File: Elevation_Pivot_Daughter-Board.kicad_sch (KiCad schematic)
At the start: 0 parts

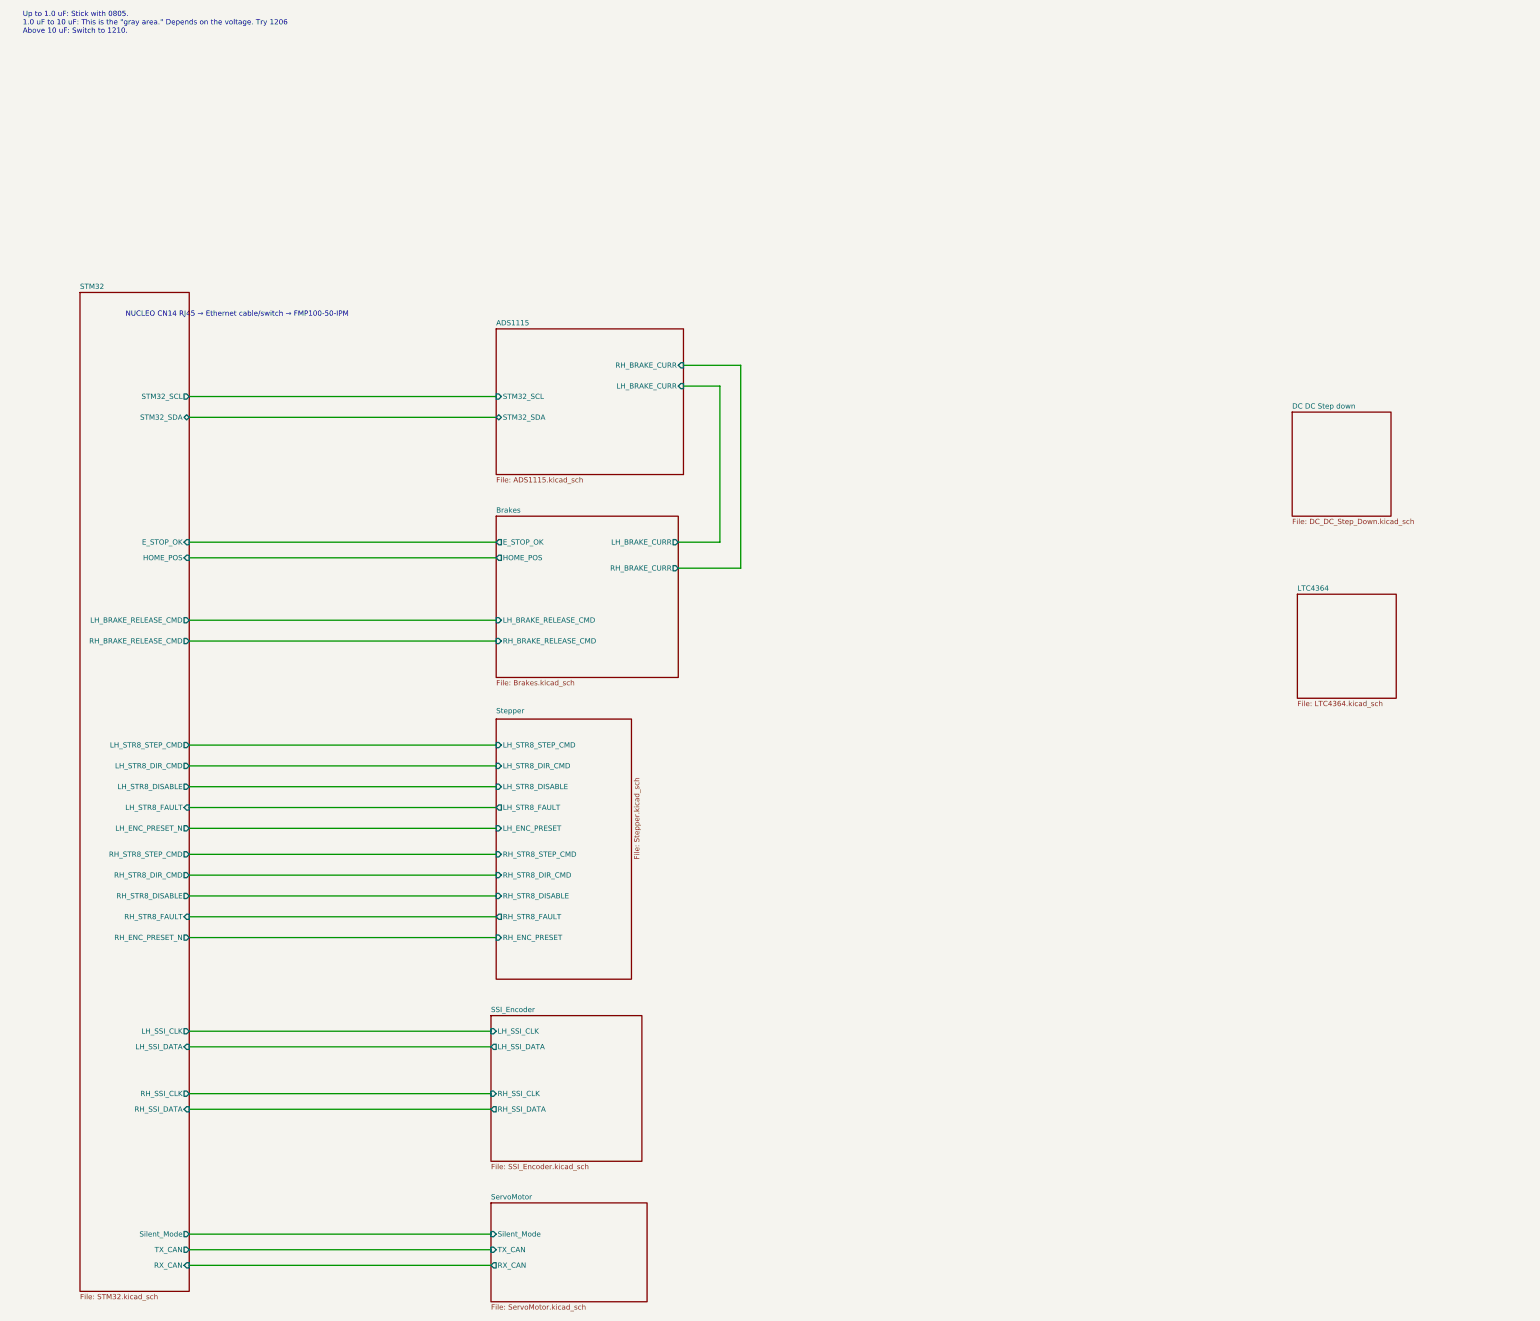
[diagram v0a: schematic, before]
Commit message: Redesign schematic for dual motor encoders
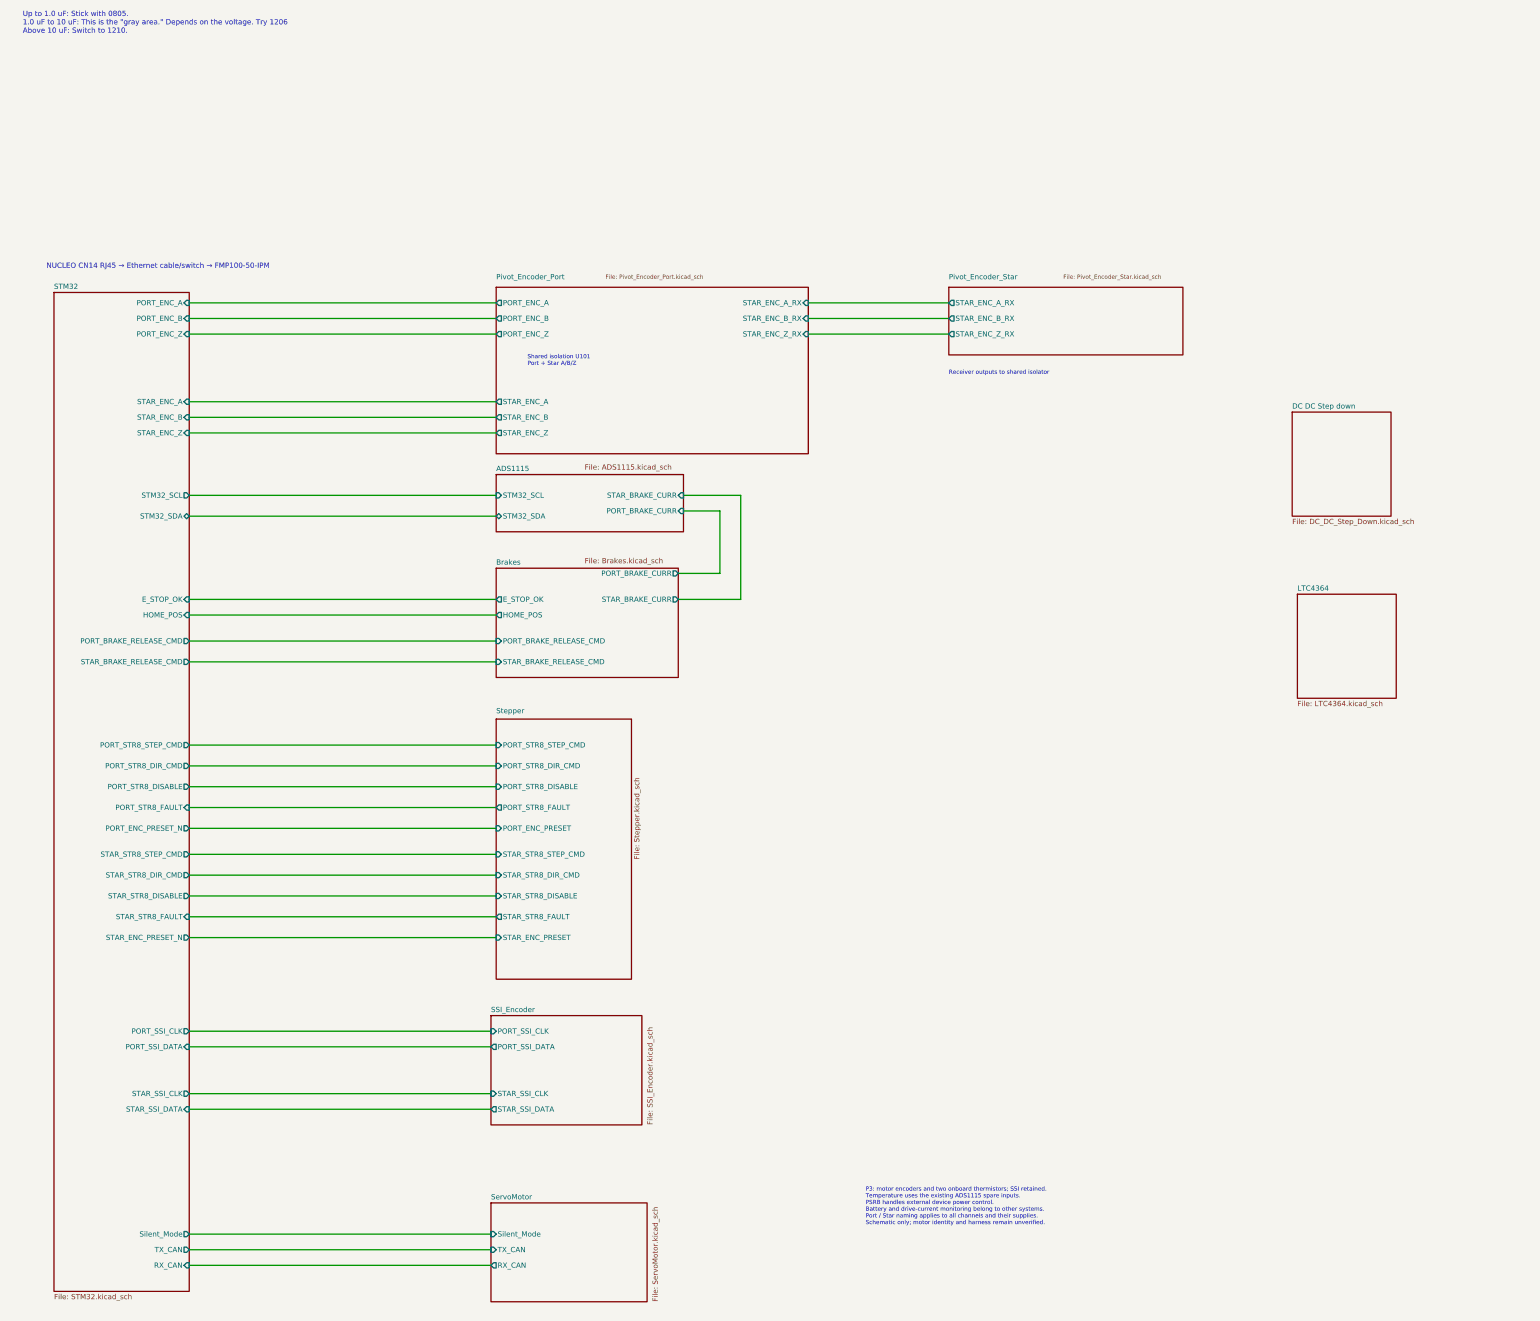
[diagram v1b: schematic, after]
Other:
- added sheet Pivot_Encoder_Port (Pivot_Encoder_Port.kicad_sch)
- added sheet Pivot_Encoder_Star (Pivot_Encoder_Star.kicad_sch)
- sheet ADS1115 ports: added PORT_BRAKE_CURR, STAR_BRAKE_CURR; removed LH_BRAKE_CURR, RH_BRAKE_CURR
- sheet Brakes ports: added PORT_BRAKE_CURR, PORT_BRAKE_RELEASE_CMD, STAR_BRAKE_CURR, STAR_BRAKE_RELEASE_CMD; removed LH_BRAKE_CURR, LH_BRAKE_RELEASE_CMD, RH_BRAKE_CURR, RH_BRAKE_RELEASE_CMD
- sheet SSI_Encoder ports: added PORT_SSI_CLK, PORT_SSI_DATA, STAR_SSI_CLK, STAR_SSI_DATA; removed LH_SSI_CLK, LH_SSI_DATA, RH_SSI_CLK, RH_SSI_DATA
- sheet STM32 ports: added PORT_BRAKE_RELEASE_CMD, PORT_ENC_A, PORT_ENC_B, PORT_ENC_PRESET_N, PORT_ENC_Z, PORT_SSI_CLK, PORT_SSI_DATA, PORT_STR8_DIR_CMD, PORT_STR8_DISABLE, PORT_STR8_FAULT, PORT_STR8_STEP_CMD, STAR_BRAKE_RELEASE_CMD, STAR_ENC_A, STAR_ENC_B, STAR_ENC_PRESET_N, STAR_ENC_Z, STAR_SSI_CLK, STAR_SSI_DATA, STAR_STR8_DIR_CMD, STAR_STR8_DISABLE, STAR_STR8_FAULT, STAR_STR8_STEP_CMD; removed LH_BRAKE_RELEASE_CMD, LH_ENC_PRESET_N, LH_SSI_CLK, LH_SSI_DATA, LH_STR8_DIR_CMD, LH_STR8_DISABLE, LH_STR8_FAULT, LH_STR8_STEP_CMD, RH_BRAKE_RELEASE_CMD, RH_ENC_PRESET_N, RH_SSI_CLK, RH_SSI_DATA, RH_STR8_DIR_CMD, RH_STR8_DISABLE, RH_STR8_FAULT, RH_STR8_STEP_CMD
- sheet Stepper ports: added PORT_ENC_PRESET, PORT_STR8_DIR_CMD, PORT_STR8_DISABLE, PORT_STR8_FAULT, PORT_STR8_STEP_CMD, STAR_ENC_PRESET, STAR_STR8_DIR_CMD, STAR_STR8_DISABLE, STAR_STR8_FAULT, STAR_STR8_STEP_CMD; removed LH_ENC_PRESET, LH_STR8_DIR_CMD, LH_STR8_DISABLE, LH_STR8_FAULT, LH_STR8_STEP_CMD, RH_ENC_PRESET, RH_STR8_DIR_CMD, RH_STR8_DISABLE, RH_STR8_FAULT, RH_STR8_STEP_CMD
- note added: "P3: motor encoders and two onboard thermistors; SSI retained. Temperature uses the existing ADS1115 spare inputs. PSRB handles external device power control. Battery and drive-current monitoring belong to other systems. Port / Star naming applies to all channels and their supplies. Schematic only; motor identity and harness remain unverified."
- note added: "Receiver outputs to shared isolator"
- note added: "Shared isolation U101 Port + Star A/B/Z"

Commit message: Preserve P5 equal-size placement, controller stack and native BOM
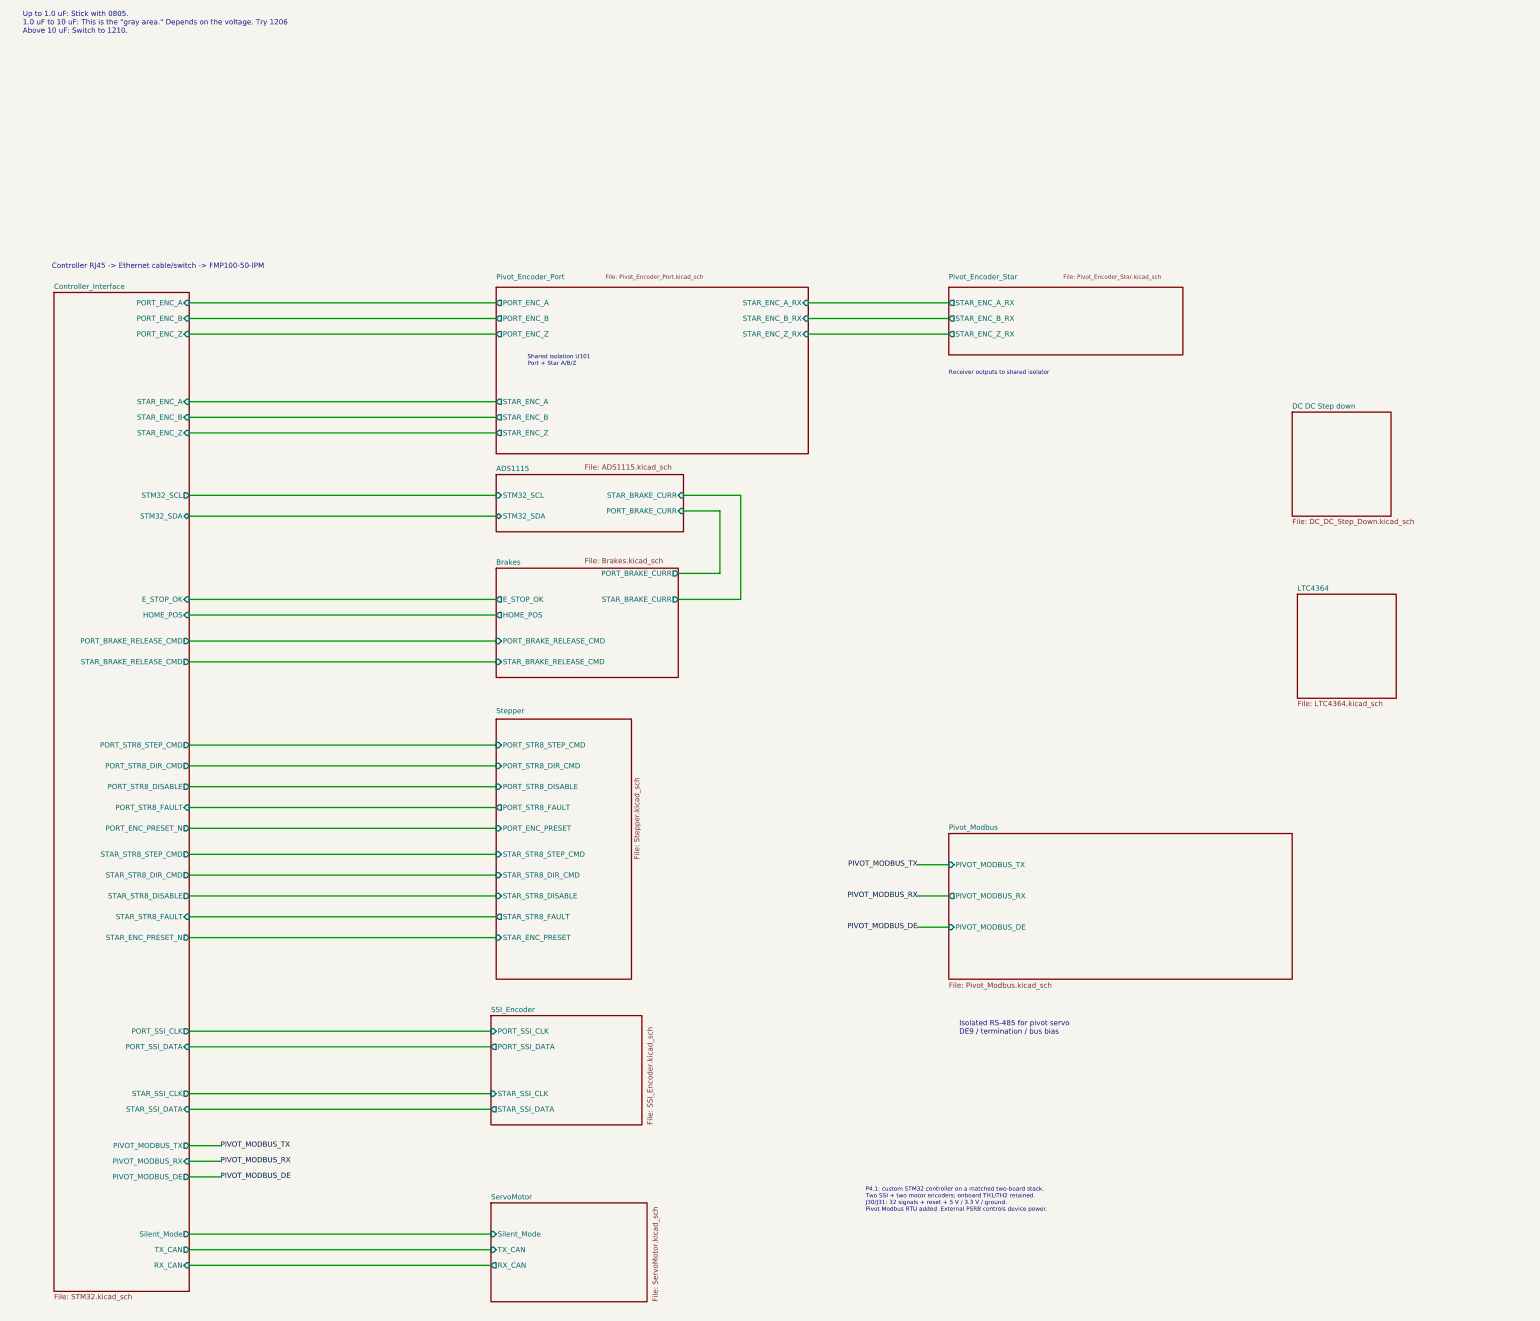
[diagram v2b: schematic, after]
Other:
- sheet STM32 renamed Controller_Interface
- added sheet Pivot_Modbus (Pivot_Modbus.kicad_sch)
- sheet Controller_Interface ports: added PIVOT_MODBUS_DE, PIVOT_MODBUS_RX, PIVOT_MODBUS_TX; removed none
- note added: "Controller RJ45 -> Ethernet cable/switch -> FMP100-50-IPM"
- note added: "Isolated RS-485 for pivot servo DE9 / termination / bus bias"
- note added: "P4.1: custom STM32 controller on a matched two-board stack. Two SSI + two motor encoders; onboard TH1/TH2 retained. J30/J31: 32 signals + reset + 5 V / 3.3 V / ground. Pivot Modbus RTU added. External PSRB controls device power."
- note removed: "NUCLEO CN14 RJ45 → Ethernet cable/switch → FMP100-50-IPM"
- note removed: "P3: motor encoders and two onboard thermistors; SSI retained. Temperature uses the existing ADS1115 spare inputs. PSRB handles external device power control. Battery and drive-current monitoring belong to other systems. Port / Star naming applies to all channels and their supplies. Schematic only; motor identity and harness remain unverified."

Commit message: Build P6 80x130 stack with redistributed SSI and stepper interfaces
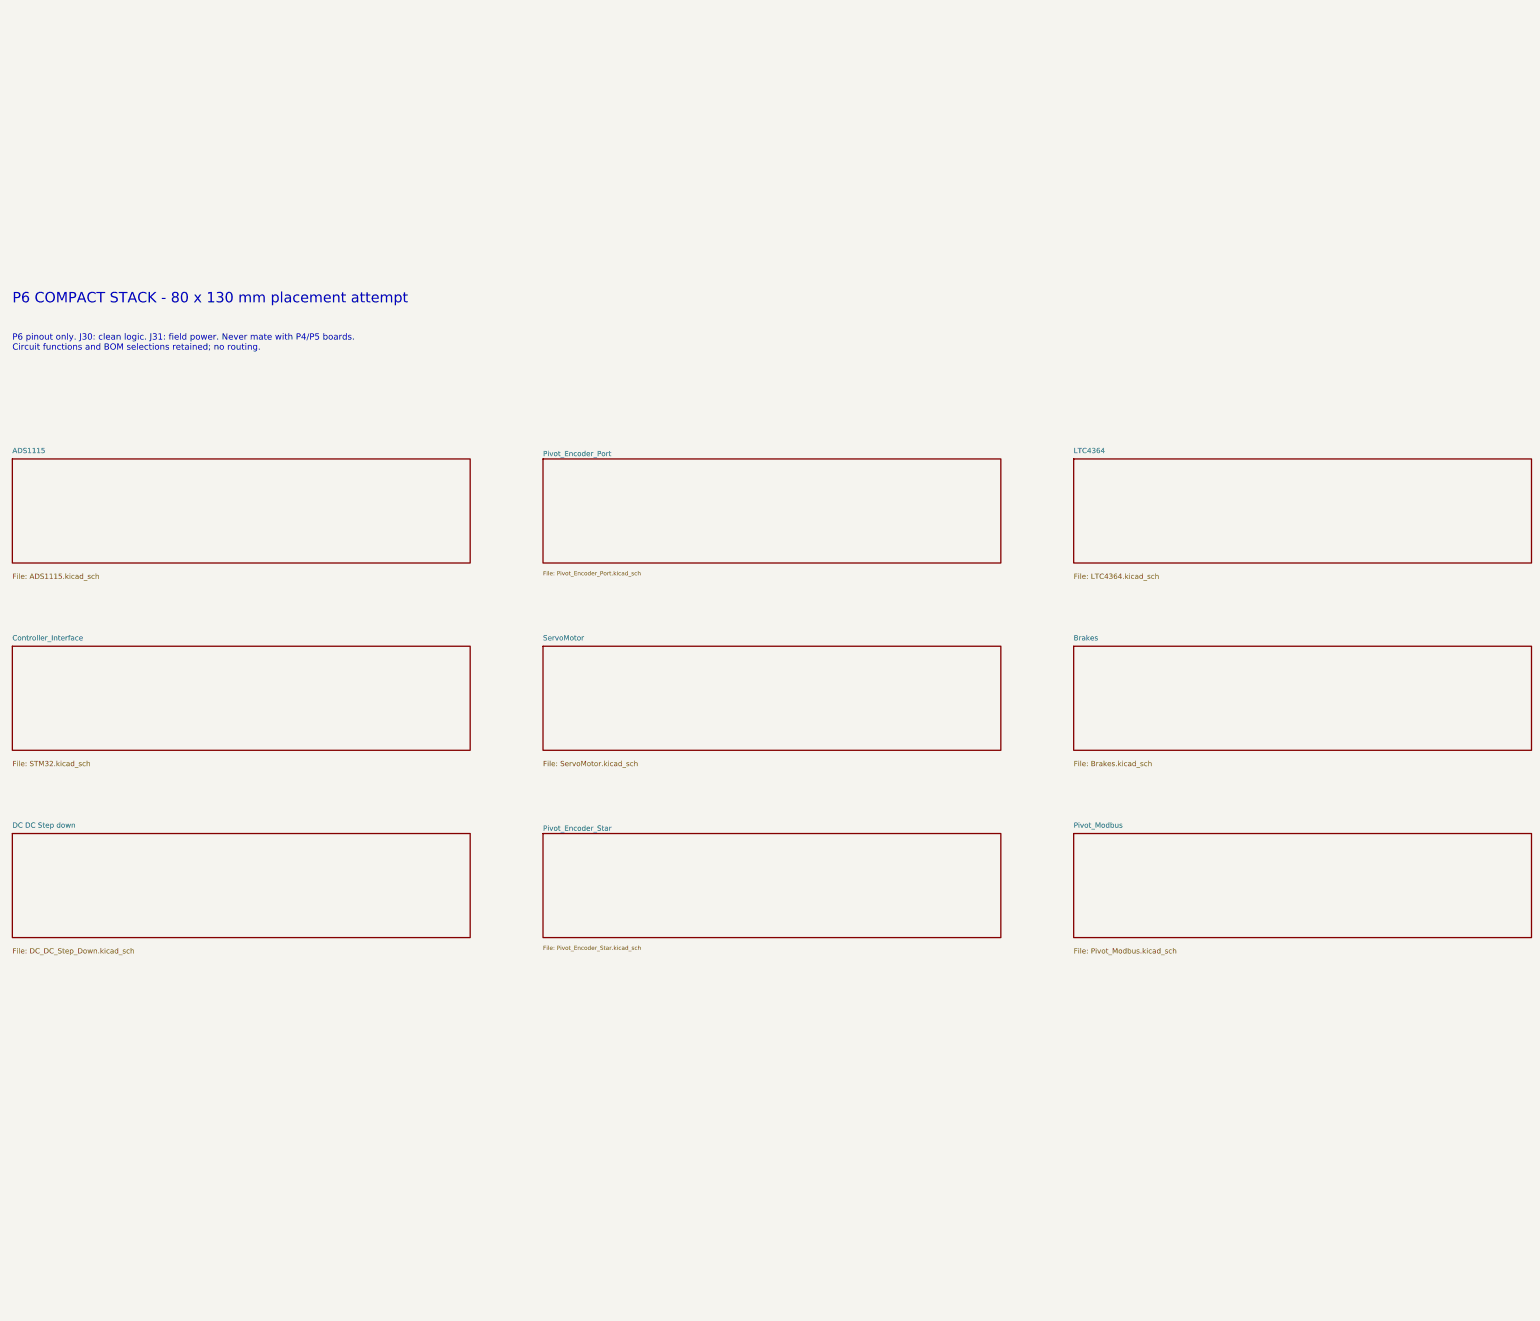
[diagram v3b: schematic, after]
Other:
- removed sheet SSI_Encoder
- removed sheet Stepper
- sheet ADS1115 ports: added none; removed PORT_BRAKE_CURR, STAR_BRAKE_CURR, STM32_SCL, STM32_SDA
- sheet Brakes ports: added none; removed E_STOP_OK, HOME_POS, PORT_BRAKE_CURR, PORT_BRAKE_RELEASE_CMD, STAR_BRAKE_CURR, STAR_BRAKE_RELEASE_CMD
- sheet Controller_Interface ports: added none; removed E_STOP_OK, HOME_POS, PIVOT_MODBUS_DE, PIVOT_MODBUS_RX, PIVOT_MODBUS_TX, PORT_BRAKE_RELEASE_CMD, PORT_ENC_A, PORT_ENC_B, PORT_ENC_PRESET_N, PORT_ENC_Z, PORT_SSI_CLK, PORT_SSI_DATA, PORT_STR8_DIR_CMD, PORT_STR8_DISABLE, PORT_STR8_FAULT, PORT_STR8_STEP_CMD, RX_CAN, STAR_BRAKE_RELEASE_CMD, STAR_ENC_A, STAR_ENC_B, STAR_ENC_PRESET_N, STAR_ENC_Z, STAR_SSI_CLK, STAR_SSI_DATA, STAR_STR8_DIR_CMD, STAR_STR8_DISABLE, STAR_STR8_FAULT, STAR_STR8_STEP_CMD, STM32_SCL, STM32_SDA, Silent_Mode, TX_CAN
- sheet Pivot_Encoder_Port ports: added none; removed PORT_ENC_A, PORT_ENC_B, PORT_ENC_Z, STAR_ENC_A, STAR_ENC_A_RX, STAR_ENC_B, STAR_ENC_B_RX, STAR_ENC_Z, STAR_ENC_Z_RX
- sheet Pivot_Encoder_Star ports: added none; removed STAR_ENC_A_RX, STAR_ENC_B_RX, STAR_ENC_Z_RX
- sheet Pivot_Modbus ports: added none; removed PIVOT_MODBUS_DE, PIVOT_MODBUS_RX, PIVOT_MODBUS_TX
- sheet ServoMotor ports: added none; removed RX_CAN, Silent_Mode, TX_CAN
- note added: "P6 COMPACT STACK - 80 x 130 mm placement attempt"
- note added: "P6 pinout only. J30: clean logic. J31: field power. Never mate with P4/P5 boards. Circuit functions and BOM selections retained; no routing."
- note removed: "Controller RJ45 -> Ethernet cable/switch -> FMP100-50-IPM"
- note removed: "Isolated RS-485 for pivot servo DE9 / termination / bus bias"
- note removed: "P4.1: custom STM32 controller on a matched two-board stack. Two SSI + two motor encoders; onboard TH1/TH2 retained. J30/J31: 32 signals + reset + 5 V / 3.3 V / ground. Pivot Modbus RTU added. External PSRB controls device power."
- note removed: "Receiver outputs to shared isolator"
- note removed: "Shared isolation U101 Port + Star A/B/Z"
- note removed: "Up to 1.0 uF: Stick with 0805. 1.0 uF to 10 uF: This is the "gray area." Depends on the voltage. Try 1206 Above 10 uF: Switch to 1210."
